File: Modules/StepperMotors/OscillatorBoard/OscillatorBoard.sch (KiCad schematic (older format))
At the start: 11 parts

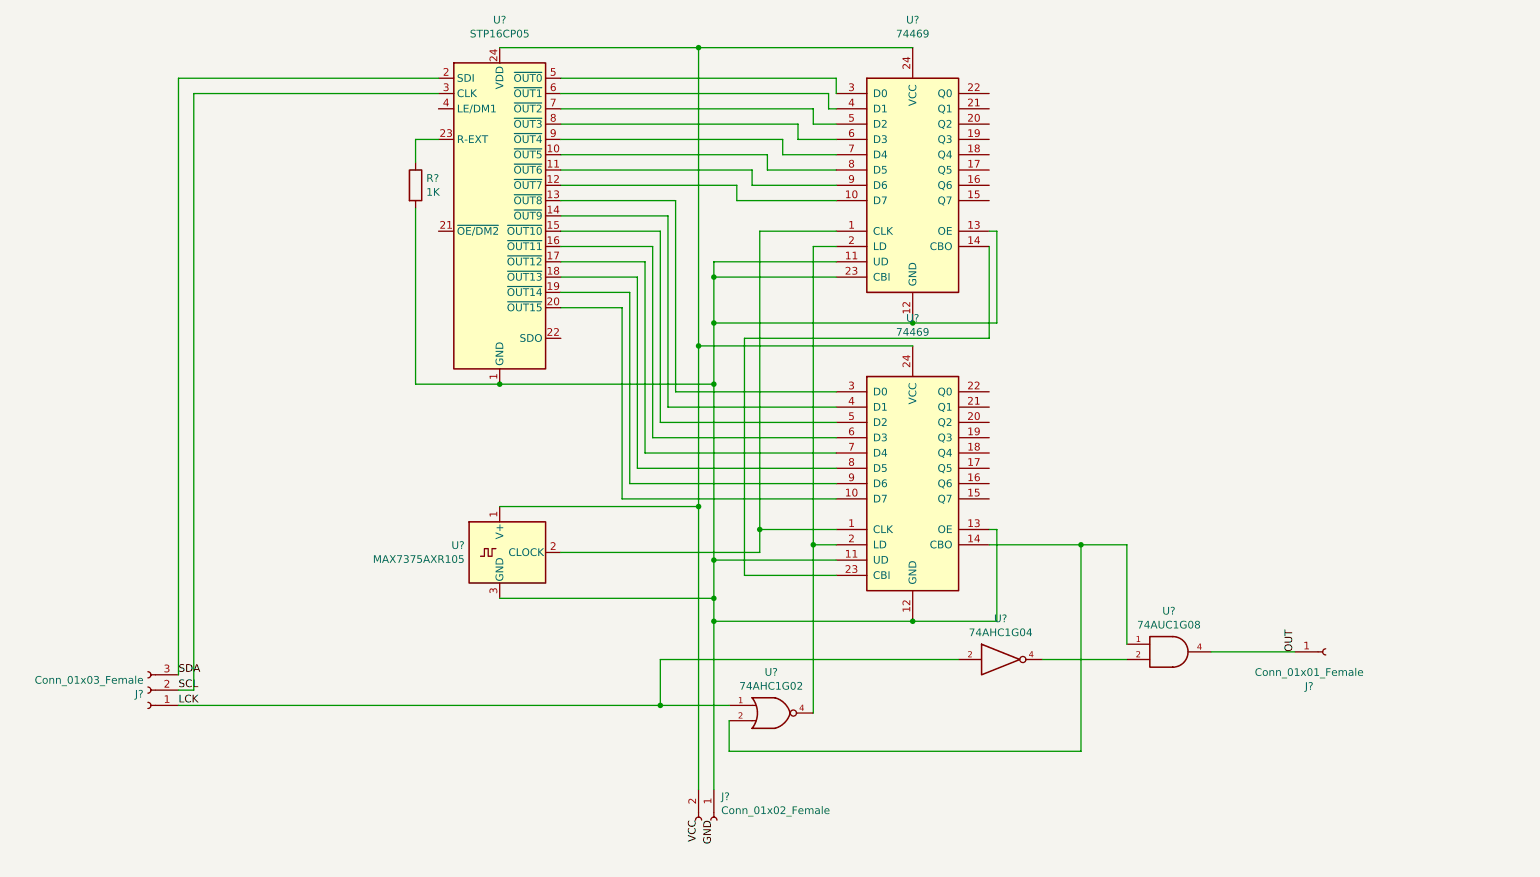
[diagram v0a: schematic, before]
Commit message: KiCAD tests (Oscillator Board)
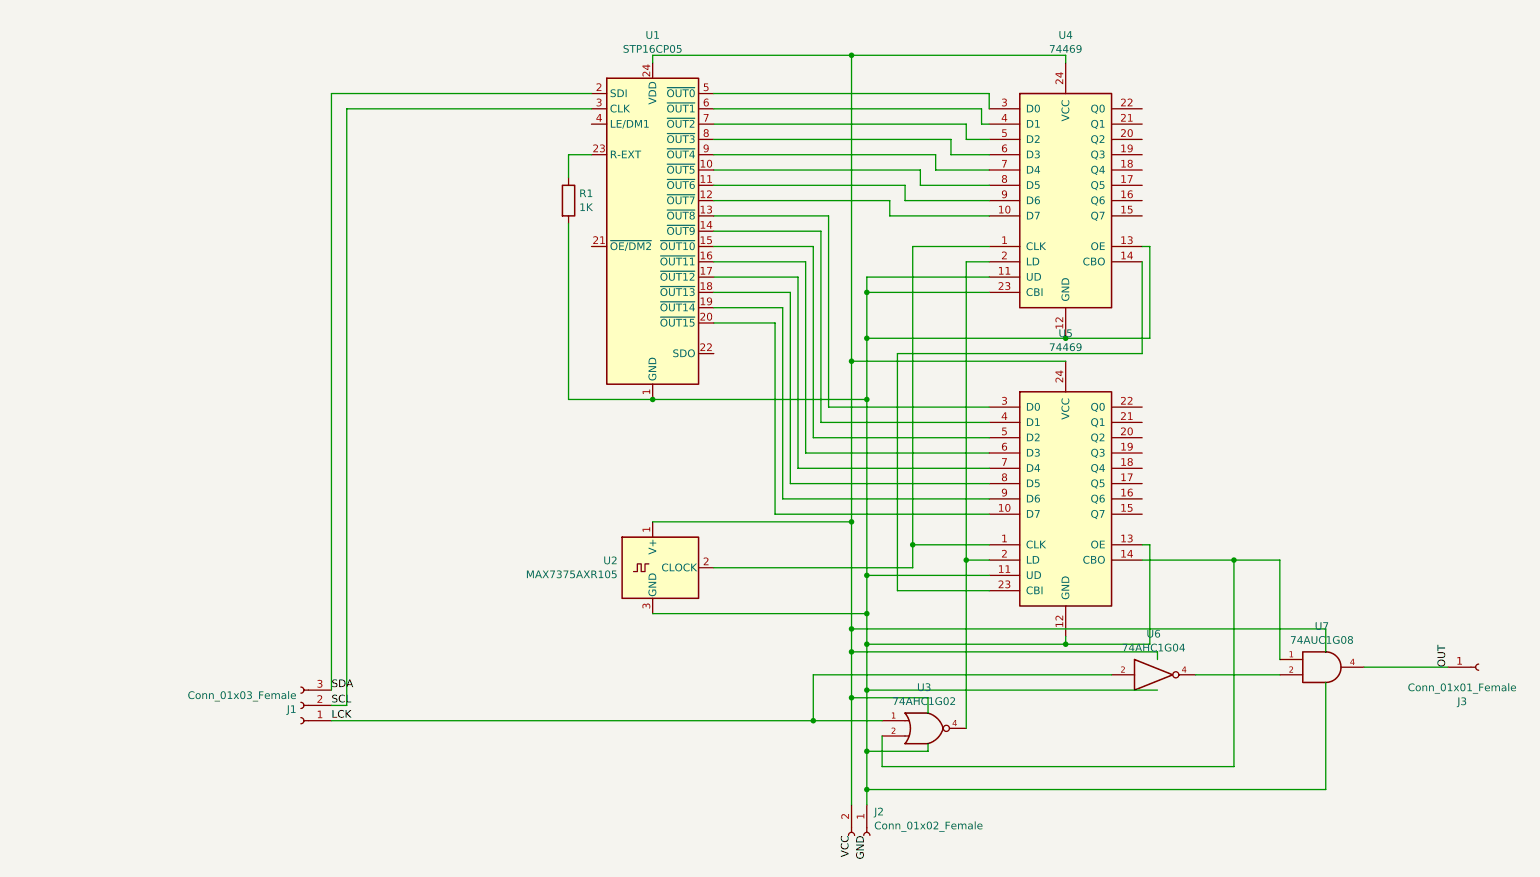
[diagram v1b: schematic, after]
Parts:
- J1: renamed from J?; footprint (none) -> Connector_PinSocket_2.00mm:PinSocket_1x03_P2.00mm_Vertical
- J2: renamed from J?; footprint (none) -> Connector_PinSocket_2.00mm:PinSocket_1x02_P2.00mm_Vertical
- J3: renamed from J?; footprint (none) -> Connector_PinSocket_2.00mm:PinSocket_1x01_P2.00mm_Vertical
- R1: renamed from R?; footprint (none) -> Resistor_THT:R_Axial_DIN0204_L3.6mm_D1.6mm_P5.08mm_Horizontal
- U1: renamed from U?; footprint (none) -> Package_SO:QSOP-24_3.9x8.7mm_P0.635mm
- U3, U7: renamed from U?; footprint (none) -> Package_TO_SOT_SMD:SOT-23-5
- U4, U5: renamed from U?; footprint (none) -> Package_DIP:DIP-24_W7.62mm
- U6: renamed from U?; footprint (none) -> Package_TO_SOT_SMD:SOT-143
- gave numbers to parts that had none: 1
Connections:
- net GND: now also J2.1 (Pin_1), R1.2, U1.1 (GND), U2.3 (GND), U4.11 (UD), U4.12 (GND), U4.13 (OE), U4.23 (CBI), U5.11 (UD), U5.12 (GND), U5.13 (OE)
- net VCC: now also J2.2 (Pin_2), U1.24 (VDD), U2.1 (V+), U4.24 (VCC), U5.24 (VCC)
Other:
- moved on the sheet: J1, J2, J3, R1, U1, U2, U3, U4, U5, U6, U7
